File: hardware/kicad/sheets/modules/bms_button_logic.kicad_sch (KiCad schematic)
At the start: 13 parts, among them Q21 L2N7002SLLT1G, SW2 TL3305AF160QG, U61 NCP718ASN330T1G, U62 PMEG10030ELPX

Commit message: fixed bugs with bms sheets
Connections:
- net PB_3V3 renamed 3v3
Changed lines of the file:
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@@
+	(wire
+		(pts
+			(xy 101.6 80.01) (xy 113.03 80.01)
+		)
+		(stroke
+			(width 0)
+			(type default)
+		)
+	)
 	(wire
 		(pts
@@
 	(wire
 		(pts
+			(xy 113.03 78.74) (xy 113.03 80.01)
+		)
+		(stroke
+			(width 0)
+			(type default)
+		)
+	)
+	(wire
+		(pts
 			(xy 91.44 116.84) (xy 91.44 110.49)
 		)
@@
 	(wire
 		(pts
-			(xy 113.03 80.01) (xy 101.6 80.01)
-		)
-		(stroke
-			(width 0)
-			(type default)
-		)
-	)
-	(wire
-		(pts
 			(xy 91.44 110.49) (xy 113.03 110.49)
 		)
@@
 			(width 0)
 			(type default)
-		)
-	)
-	(label "PB_3V3"
-		(at 116.84 80.01 0)
-		(effects
-			(font
-				(size 1.27 1.27)
-			)
-			(justify left bottom)
 		)
 	)
@@
 		)
 	)
+	(hierarchical_label "3v3"
+		(shape output)
+		(at 113.03 78.74 90)
+		(effects
+			(font
+				(size 1.27 1.27)
+			)
+			(justify left)
+		)
+	)

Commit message: various improvements
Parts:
- renumbered C112 to C120, C115 to C121, C118 to C122, D35 to D43, Q21 to Q25, R162 to R182, R174 to R183, R177 to R184, R178 to R185, U61 to U62, U62 to U63
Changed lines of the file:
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@@
 		(on_board yes)
 		(dnp no)
-		(property "Reference" "R174"
+		(property "Reference" "R183"
 			(at 161.29 124.46 90)
 			(effects
@@
 			(project "svea_powerboard_rev3"
 				(path "/3f85abf4-0b95-4c4a-b7e9-06f59ca1ea3d/5c2e021f-c2d4-49e2-8c36-9a64f1f12001/261b4c59-ebc7-47a2-bb10-0e71ece0f9bf"
-					(reference "R174")
+					(reference "R183")
 					(unit 1)
 				)
@@
 		(on_board yes)
 		(dnp no)
-		(property "Reference" "D35"
+		(property "Reference" "D43"
 			(at 175.26 124.46 90)
 			(effects
@@
 			(project "svea_powerboard_rev3"
 				(path "/3f85abf4-0b95-4c4a-b7e9-06f59ca1ea3d/5c2e021f-c2d4-49e2-8c36-9a64f1f12001/261b4c59-ebc7-47a2-bb10-0e71ece0f9bf"
-					(reference "D35")
+					(reference "D43")
 					(unit 1)
 				)
@@
 		(on_board yes)
 		(dnp no)
-		(property "Reference" "R178"
+		(property "Reference" "R185"
 			(at 209.55 124.46 90)
 			(effects
@@
 			(project "svea_powerboard_rev3"
 				(path "/3f85abf4-0b95-4c4a-b7e9-06f59ca1ea3d/5c2e021f-c2d4-49e2-8c36-9a64f1f12001/261b4c59-ebc7-47a2-bb10-0e71ece0f9bf"
-					(reference "R178")
+					(reference "R185")
 					(unit 1)
 				)
@@
 		(on_board yes)
 		(dnp no)
-		(property "Reference" "C112"
+		(property "Reference" "C120"
 			(at 64.77 96.52 90)
 			(effects
@@
 			(project "svea_powerboard_rev3"
 				(path "/3f85abf4-0b95-4c4a-b7e9-06f59ca1ea3d/5c2e021f-c2d4-49e2-8c36-9a64f1f12001/261b4c59-ebc7-47a2-bb10-0e71ece0f9bf"
-					(reference "C112")
+					(reference "C120")
 					(unit 1)
 				)
@@
 		(on_board yes)
 		(dnp no)
-		(property "Reference" "U61"
+		(property "Reference" "U62"
 			(at 81.28 76.2 0)
 			(effects
@@
 			(project "svea_powerboard_rev3"
 				(path "/3f85abf4-0b95-4c4a-b7e9-06f59ca1ea3d/5c2e021f-c2d4-49e2-8c36-9a64f1f12001/261b4c59-ebc7-47a2-bb10-0e71ece0f9bf"
-					(reference "U61")
+					(reference "U62")
 					(unit 1)
 				)
@@
 		(on_board yes)
 		(dnp no)
-		(property "Reference" "R162"
+		(property "Reference" "R182"
 			(at 78.74 97.79 90)
 			(effects
@@
 			(project "svea_powerboard_rev3"
 				(path "/3f85abf4-0b95-4c4a-b7e9-06f59ca1ea3d/5c2e021f-c2d4-49e2-8c36-9a64f1f12001/261b4c59-ebc7-47a2-bb10-0e71ece0f9bf"
-					(reference "R162")
+					(reference "R182")
 					(unit 1)
 				)
@@
 		(on_board yes)
 		(dnp no)
-		(property "Reference" "C118"
+		(property "Reference" "C122"
 			(at 190.5 124.46 90)
 			(effects
@@
 			(project "svea_powerboard_rev3"
 				(path "/3f85abf4-0b95-4c4a-b7e9-06f59ca1ea3d/5c2e021f-c2d4-49e2-8c36-9a64f1f12001/261b4c59-ebc7-47a2-bb10-0e71ece0f9bf"
-					(reference "C118")
+					(reference "C122")
 					(unit 1)
 				)
@@
 		(on_board yes)
 		(dnp no)
-		(property "Reference" "U62"
+		(property "Reference" "U63"
 			(at 144.78 74.93 0)
 			(effects
@@
 			(project "svea_powerboard_rev3"
 				(path "/3f85abf4-0b95-4c4a-b7e9-06f59ca1ea3d/5c2e021f-c2d4-49e2-8c36-9a64f1f12001/261b4c59-ebc7-47a2-bb10-0e71ece0f9bf"
-					(reference "U62")
+					(reference "U63")
 					(unit 1)
 				)
@@
 		(on_board yes)
 		(dnp no)
-		(property "Reference" "R177"
+		(property "Reference" "R184"
 			(at 209.55 68.58 90)
 			(effects
@@
 			(project "svea_powerboard_rev3"
 				(path "/3f85abf4-0b95-4c4a-b7e9-06f59ca1ea3d/5c2e021f-c2d4-49e2-8c36-9a64f1f12001/261b4c59-ebc7-47a2-bb10-0e71ece0f9bf"
-					(reference "R177")
+					(reference "R184")
 					(unit 1)
 				)
@@
 		(on_board yes)
 		(dnp no)
-		(property "Reference" "C115"
+		(property "Reference" "C121"
 			(at 116.84 93.98 90)
 			(effects
@@
 			(project "svea_powerboard_rev3"
 				(path "/3f85abf4-0b95-4c4a-b7e9-06f59ca1ea3d/5c2e021f-c2d4-49e2-8c36-9a64f1f12001/261b4c59-ebc7-47a2-bb10-0e71ece0f9bf"
-					(reference "C115")
+					(reference "C121")
 					(unit 1)
 				)
@@
 		(on_board yes)
 		(dnp no)
-		(property "Reference" "Q21"
+		(property "Reference" "Q25"
 			(at 179.07 90.17 0)
 			(effects
@@
 			(project "svea_powerboard_rev3"
 				(path "/3f85abf4-0b95-4c4a-b7e9-06f59ca1ea3d/5c2e021f-c2d4-49e2-8c36-9a64f1f12001/261b4c59-ebc7-47a2-bb10-0e71ece0f9bf"
-					(reference "Q21")
+					(reference "Q25")
 					(unit 1)
 				)

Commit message: various improvements
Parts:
- renumbered C120 to C108, C121 to C113, C122 to C116, D43 to D32, Q25 to Q20, R182 to R162, R183 to R164, R184 to R166, R185 to R167, U62 to U63, U63 to U65
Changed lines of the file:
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@@
 		(on_board yes)
 		(dnp no)
-		(property "Reference" "R183"
+		(property "Reference" "R164"
 			(at 161.29 124.46 90)
 			(effects
@@
 			(project "svea_powerboard_rev3"
 				(path "/3f85abf4-0b95-4c4a-b7e9-06f59ca1ea3d/5c2e021f-c2d4-49e2-8c36-9a64f1f12001/261b4c59-ebc7-47a2-bb10-0e71ece0f9bf"
-					(reference "R183")
+					(reference "R164")
 					(unit 1)
 				)
@@
 		(on_board yes)
 		(dnp no)
-		(property "Reference" "D43"
+		(property "Reference" "D32"
 			(at 175.26 124.46 90)
 			(effects
@@
 			(project "svea_powerboard_rev3"
 				(path "/3f85abf4-0b95-4c4a-b7e9-06f59ca1ea3d/5c2e021f-c2d4-49e2-8c36-9a64f1f12001/261b4c59-ebc7-47a2-bb10-0e71ece0f9bf"
-					(reference "D43")
+					(reference "D32")
 					(unit 1)
 				)
@@
 		(on_board yes)
 		(dnp no)
-		(property "Reference" "R185"
+		(property "Reference" "R167"
 			(at 209.55 124.46 90)
 			(effects
@@
 			(project "svea_powerboard_rev3"
 				(path "/3f85abf4-0b95-4c4a-b7e9-06f59ca1ea3d/5c2e021f-c2d4-49e2-8c36-9a64f1f12001/261b4c59-ebc7-47a2-bb10-0e71ece0f9bf"
-					(reference "R185")
+					(reference "R167")
 					(unit 1)
 				)
@@
 		(on_board yes)
 		(dnp no)
-		(property "Reference" "C120"
+		(property "Reference" "C108"
 			(at 64.77 96.52 90)
 			(effects
@@
 			(project "svea_powerboard_rev3"
 				(path "/3f85abf4-0b95-4c4a-b7e9-06f59ca1ea3d/5c2e021f-c2d4-49e2-8c36-9a64f1f12001/261b4c59-ebc7-47a2-bb10-0e71ece0f9bf"
-					(reference "C120")
+					(reference "C108")
 					(unit 1)
 				)
@@
 		(on_board yes)
 		(dnp no)
-		(property "Reference" "U62"
+		(property "Reference" "U63"
 			(at 81.28 76.2 0)
 			(effects
@@
 			(project "svea_powerboard_rev3"
 				(path "/3f85abf4-0b95-4c4a-b7e9-06f59ca1ea3d/5c2e021f-c2d4-49e2-8c36-9a64f1f12001/261b4c59-ebc7-47a2-bb10-0e71ece0f9bf"
-					(reference "U62")
+					(reference "U63")
 					(unit 1)
 				)
@@
 		(on_board yes)
 		(dnp no)
-		(property "Reference" "R182"
+		(property "Reference" "R162"
 			(at 78.74 97.79 90)
 			(effects
@@
 			(project "svea_powerboard_rev3"
 				(path "/3f85abf4-0b95-4c4a-b7e9-06f59ca1ea3d/5c2e021f-c2d4-49e2-8c36-9a64f1f12001/261b4c59-ebc7-47a2-bb10-0e71ece0f9bf"
-					(reference "R182")
+					(reference "R162")
 					(unit 1)
 				)
@@
 		(on_board yes)
 		(dnp no)
-		(property "Reference" "C122"
+		(property "Reference" "C116"
 			(at 190.5 124.46 90)
 			(effects
@@
 			(project "svea_powerboard_rev3"
 				(path "/3f85abf4-0b95-4c4a-b7e9-06f59ca1ea3d/5c2e021f-c2d4-49e2-8c36-9a64f1f12001/261b4c59-ebc7-47a2-bb10-0e71ece0f9bf"
-					(reference "C122")
+					(reference "C116")
 					(unit 1)
 				)
@@
 		(on_board yes)
 		(dnp no)
-		(property "Reference" "U63"
+		(property "Reference" "U65"
 			(at 144.78 74.93 0)
 			(effects
@@
 			(project "svea_powerboard_rev3"
 				(path "/3f85abf4-0b95-4c4a-b7e9-06f59ca1ea3d/5c2e021f-c2d4-49e2-8c36-9a64f1f12001/261b4c59-ebc7-47a2-bb10-0e71ece0f9bf"
-					(reference "U63")
+					(reference "U65")
 					(unit 1)
 				)
@@
 		(on_board yes)
 		(dnp no)
-		(property "Reference" "R184"
+		(property "Reference" "R166"
 			(at 209.55 68.58 90)
 			(effects
@@
 			(project "svea_powerboard_rev3"
 				(path "/3f85abf4-0b95-4c4a-b7e9-06f59ca1ea3d/5c2e021f-c2d4-49e2-8c36-9a64f1f12001/261b4c59-ebc7-47a2-bb10-0e71ece0f9bf"
-					(reference "R184")
+					(reference "R166")
 					(unit 1)
 				)
@@
 		(on_board yes)
 		(dnp no)
-		(property "Reference" "C121"
+		(property "Reference" "C113"
 			(at 116.84 93.98 90)
 			(effects
@@
 			(project "svea_powerboard_rev3"
 				(path "/3f85abf4-0b95-4c4a-b7e9-06f59ca1ea3d/5c2e021f-c2d4-49e2-8c36-9a64f1f12001/261b4c59-ebc7-47a2-bb10-0e71ece0f9bf"
-					(reference "C121")
+					(reference "C113")
 					(unit 1)
 				)
@@
 		(on_board yes)
 		(dnp no)
-		(property "Reference" "Q25"
+		(property "Reference" "Q20"
 			(at 179.07 90.17 0)
 			(effects
@@
 			(project "svea_powerboard_rev3"
 				(path "/3f85abf4-0b95-4c4a-b7e9-06f59ca1ea3d/5c2e021f-c2d4-49e2-8c36-9a64f1f12001/261b4c59-ebc7-47a2-bb10-0e71ece0f9bf"
-					(reference "Q25")
+					(reference "Q20")
 					(unit 1)
 				)

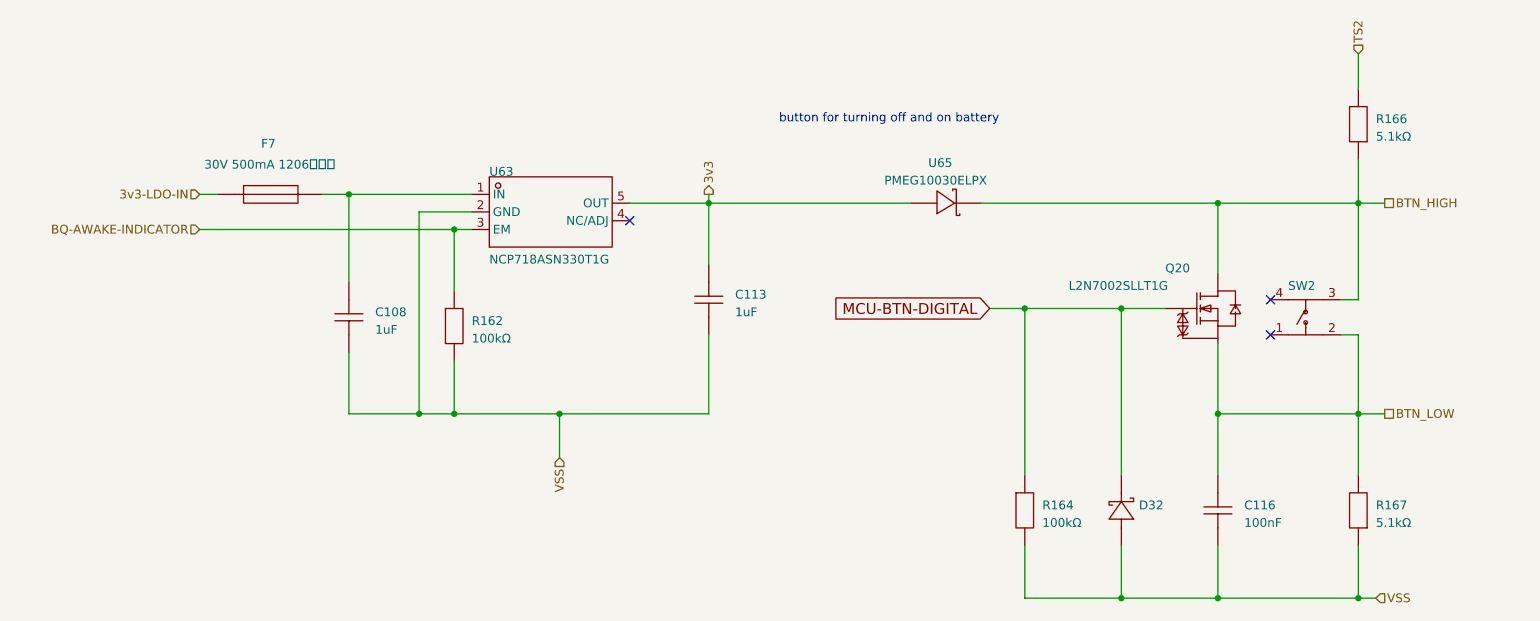
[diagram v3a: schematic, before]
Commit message: current sensing on the servos and cleaning up empty sheets
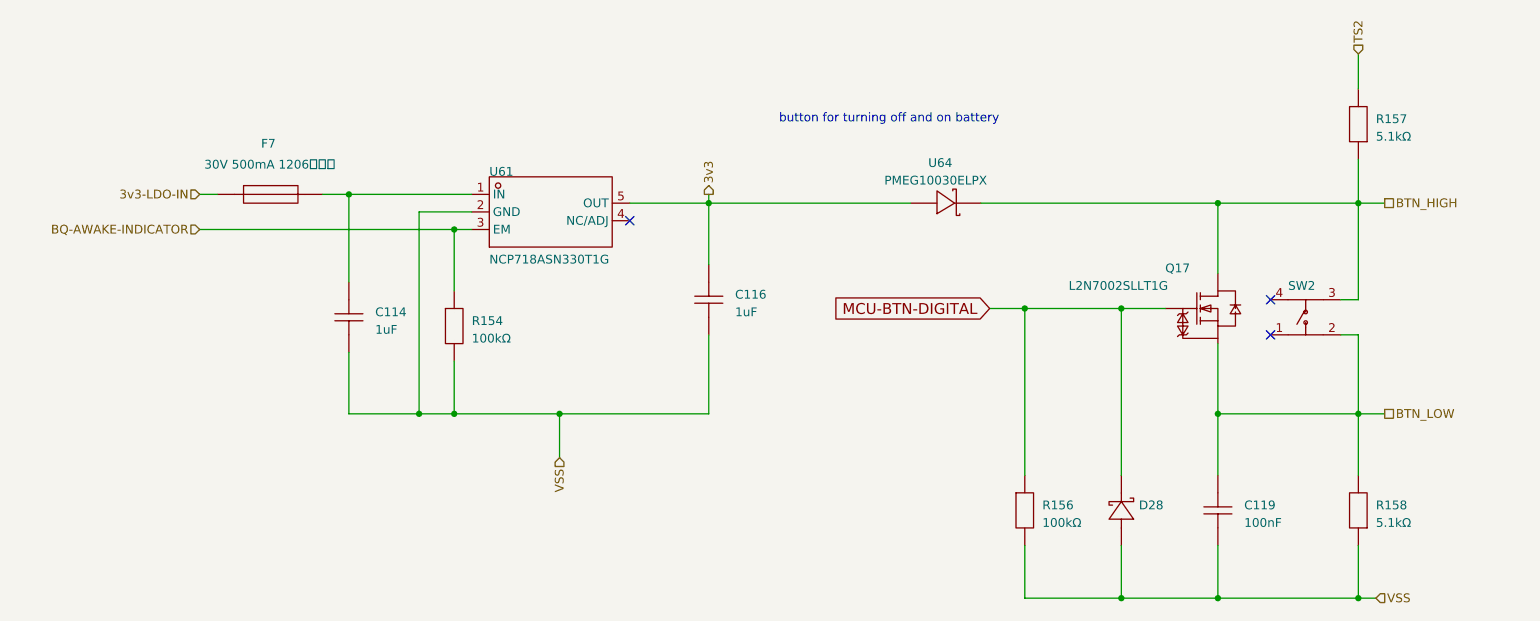
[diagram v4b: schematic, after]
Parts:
- renumbered C108 to C114, C113 to C116, C116 to C119, D32 to D28, Q20 to Q17, R162 to R154, R164 to R156, R166 to R157, R167 to R158, U63 to U61, U65 to U64
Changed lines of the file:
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@@
 		(on_board yes)
 		(dnp no)
-		(property "Reference" "R164"
+		(property "Reference" "R156"
 			(at 161.29 124.46 90)
 			(effects
@@
 			(project "svea_powerboard_rev3"
 				(path "/3f85abf4-0b95-4c4a-b7e9-06f59ca1ea3d/5c2e021f-c2d4-49e2-8c36-9a64f1f12001/261b4c59-ebc7-47a2-bb10-0e71ece0f9bf"
-					(reference "R164")
+					(reference "R156")
 					(unit 1)
 				)
@@
 		(on_board yes)
 		(dnp no)
-		(property "Reference" "D32"
+		(property "Reference" "D28"
 			(at 175.26 124.46 90)
 			(effects
@@
 			(project "svea_powerboard_rev3"
 				(path "/3f85abf4-0b95-4c4a-b7e9-06f59ca1ea3d/5c2e021f-c2d4-49e2-8c36-9a64f1f12001/261b4c59-ebc7-47a2-bb10-0e71ece0f9bf"
-					(reference "D32")
+					(reference "D28")
 					(unit 1)
 				)
@@
 		(on_board yes)
 		(dnp no)
-		(property "Reference" "R167"
+		(property "Reference" "R158"
 			(at 209.55 124.46 90)
 			(effects
@@
 			(project "svea_powerboard_rev3"
 				(path "/3f85abf4-0b95-4c4a-b7e9-06f59ca1ea3d/5c2e021f-c2d4-49e2-8c36-9a64f1f12001/261b4c59-ebc7-47a2-bb10-0e71ece0f9bf"
-					(reference "R167")
+					(reference "R158")
 					(unit 1)
 				)
@@
 		(on_board yes)
 		(dnp no)
-		(property "Reference" "C108"
+		(property "Reference" "C114"
 			(at 64.77 96.52 90)
 			(effects
@@
 			(project "svea_powerboard_rev3"
 				(path "/3f85abf4-0b95-4c4a-b7e9-06f59ca1ea3d/5c2e021f-c2d4-49e2-8c36-9a64f1f12001/261b4c59-ebc7-47a2-bb10-0e71ece0f9bf"
-					(reference "C108")
+					(reference "C114")
 					(unit 1)
 				)
@@
 		(on_board yes)
 		(dnp no)
-		(property "Reference" "U63"
+		(property "Reference" "U61"
 			(at 81.28 76.2 0)
 			(effects
@@
 			(project "svea_powerboard_rev3"
 				(path "/3f85abf4-0b95-4c4a-b7e9-06f59ca1ea3d/5c2e021f-c2d4-49e2-8c36-9a64f1f12001/261b4c59-ebc7-47a2-bb10-0e71ece0f9bf"
-					(reference "U63")
+					(reference "U61")
 					(unit 1)
 				)
@@
 		(on_board yes)
 		(dnp no)
-		(property "Reference" "R162"
+		(property "Reference" "R154"
 			(at 78.74 97.79 90)
 			(effects
@@
 			(project "svea_powerboard_rev3"
 				(path "/3f85abf4-0b95-4c4a-b7e9-06f59ca1ea3d/5c2e021f-c2d4-49e2-8c36-9a64f1f12001/261b4c59-ebc7-47a2-bb10-0e71ece0f9bf"
-					(reference "R162")
+					(reference "R154")
 					(unit 1)
 				)
@@
 		(on_board yes)
 		(dnp no)
-		(property "Reference" "C116"
+		(property "Reference" "C119"
 			(at 190.5 124.46 90)
 			(effects
@@
 			(project "svea_powerboard_rev3"
 				(path "/3f85abf4-0b95-4c4a-b7e9-06f59ca1ea3d/5c2e021f-c2d4-49e2-8c36-9a64f1f12001/261b4c59-ebc7-47a2-bb10-0e71ece0f9bf"
-					(reference "C116")
+					(reference "C119")
 					(unit 1)
 				)
@@
 		(on_board yes)
 		(dnp no)
-		(property "Reference" "U65"
+		(property "Reference" "U64"
 			(at 144.78 74.93 0)
 			(effects
@@
 			(project "svea_powerboard_rev3"
 				(path "/3f85abf4-0b95-4c4a-b7e9-06f59ca1ea3d/5c2e021f-c2d4-49e2-8c36-9a64f1f12001/261b4c59-ebc7-47a2-bb10-0e71ece0f9bf"
-					(reference "U65")
+					(reference "U64")
 					(unit 1)
 				)
@@
 		(on_board yes)
 		(dnp no)
-		(property "Reference" "R166"
+		(property "Reference" "R157"
 			(at 209.55 68.58 90)
 			(effects
@@
 			(project "svea_powerboard_rev3"
 				(path "/3f85abf4-0b95-4c4a-b7e9-06f59ca1ea3d/5c2e021f-c2d4-49e2-8c36-9a64f1f12001/261b4c59-ebc7-47a2-bb10-0e71ece0f9bf"
-					(reference "R166")
+					(reference "R157")
 					(unit 1)
 				)
@@
 		(on_board yes)
 		(dnp no)
-		(property "Reference" "C113"
+		(property "Reference" "C116"
 			(at 116.84 93.98 90)
 			(effects
@@
 			(project "svea_powerboard_rev3"
 				(path "/3f85abf4-0b95-4c4a-b7e9-06f59ca1ea3d/5c2e021f-c2d4-49e2-8c36-9a64f1f12001/261b4c59-ebc7-47a2-bb10-0e71ece0f9bf"
-					(reference "C113")
+					(reference "C116")
 					(unit 1)
 				)
@@
 		(on_board yes)
 		(dnp no)
-		(property "Reference" "Q20"
+		(property "Reference" "Q17"
 			(at 179.07 90.17 0)
 			(effects
@@
 			(project "svea_powerboard_rev3"
 				(path "/3f85abf4-0b95-4c4a-b7e9-06f59ca1ea3d/5c2e021f-c2d4-49e2-8c36-9a64f1f12001/261b4c59-ebc7-47a2-bb10-0e71ece0f9bf"
-					(reference "Q20")
+					(reference "Q17")
 					(unit 1)
 				)

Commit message: new references
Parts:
- renumbered C114 to C129, C116 to C131, C119 to C133, D28 to D38, F7 to F5, Q17 to Q18, R154 to R177, R156 to R178, R157 to R179, R158 to R180, SW2 to SW1, U64 to U63
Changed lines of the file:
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@@
 		(on_board yes)
 		(dnp no)
-		(property "Reference" "R156"
+		(property "Reference" "R178"
 			(at 161.29 124.46 90)
 			(effects
@@
 			(project "svea_powerboard_rev3"
 				(path "/3f85abf4-0b95-4c4a-b7e9-06f59ca1ea3d/5c2e021f-c2d4-49e2-8c36-9a64f1f12001/261b4c59-ebc7-47a2-bb10-0e71ece0f9bf"
-					(reference "R156")
+					(reference "R178")
 					(unit 1)
 				)
@@
 		(on_board yes)
 		(dnp no)
-		(property "Reference" "SW2"
+		(property "Reference" "SW1"
 			(at 196.85 92.71 0)
 			(effects
@@
 			(project "svea_powerboard_rev3"
 				(path "/3f85abf4-0b95-4c4a-b7e9-06f59ca1ea3d/5c2e021f-c2d4-49e2-8c36-9a64f1f12001/261b4c59-ebc7-47a2-bb10-0e71ece0f9bf"
-					(reference "SW2")
+					(reference "SW1")
 					(unit 1)
 				)
@@
 		(on_board yes)
 		(dnp no)
-		(property "Reference" "D28"
+		(property "Reference" "D38"
 			(at 175.26 124.46 90)
 			(effects
@@
 			(project "svea_powerboard_rev3"
 				(path "/3f85abf4-0b95-4c4a-b7e9-06f59ca1ea3d/5c2e021f-c2d4-49e2-8c36-9a64f1f12001/261b4c59-ebc7-47a2-bb10-0e71ece0f9bf"
-					(reference "D28")
+					(reference "D38")
 					(unit 1)
 				)
@@
 		(on_board yes)
 		(dnp no)
-		(property "Reference" "R158"
+		(property "Reference" "R180"
 			(at 209.55 124.46 90)
 			(effects
@@
 			(project "svea_powerboard_rev3"
 				(path "/3f85abf4-0b95-4c4a-b7e9-06f59ca1ea3d/5c2e021f-c2d4-49e2-8c36-9a64f1f12001/261b4c59-ebc7-47a2-bb10-0e71ece0f9bf"
-					(reference "R158")
+					(reference "R180")
 					(unit 1)
 				)
@@
 		(on_board yes)
 		(dnp no)
-		(property "Reference" "C114"
+		(property "Reference" "C129"
 			(at 64.77 96.52 90)
 			(effects
@@
 			(project "svea_powerboard_rev3"
 				(path "/3f85abf4-0b95-4c4a-b7e9-06f59ca1ea3d/5c2e021f-c2d4-49e2-8c36-9a64f1f12001/261b4c59-ebc7-47a2-bb10-0e71ece0f9bf"
-					(reference "C114")
+					(reference "C129")
 					(unit 1)
 				)
@@
 		(on_board yes)
 		(dnp no)
-		(property "Reference" "R154"
+		(property "Reference" "R177"
 			(at 78.74 97.79 90)
 			(effects
@@
 			(project "svea_powerboard_rev3"
 				(path "/3f85abf4-0b95-4c4a-b7e9-06f59ca1ea3d/5c2e021f-c2d4-49e2-8c36-9a64f1f12001/261b4c59-ebc7-47a2-bb10-0e71ece0f9bf"
-					(reference "R154")
+					(reference "R177")
 					(unit 1)
 				)
@@
 		(on_board yes)
 		(dnp no)
-		(property "Reference" "C119"
+		(property "Reference" "C133"
 			(at 190.5 124.46 90)
 			(effects
@@
 			(project "svea_powerboard_rev3"
 				(path "/3f85abf4-0b95-4c4a-b7e9-06f59ca1ea3d/5c2e021f-c2d4-49e2-8c36-9a64f1f12001/261b4c59-ebc7-47a2-bb10-0e71ece0f9bf"
-					(reference "C119")
+					(reference "C133")
 					(unit 1)
 				)
@@
 		(on_board yes)
 		(dnp no)
-		(property "Reference" "F7"
+		(property "Reference" "F5"
 			(at 48.26 72.136 0)
 			(effects
@@
 			(project "svea_powerboard_rev3"
 				(path "/3f85abf4-0b95-4c4a-b7e9-06f59ca1ea3d/5c2e021f-c2d4-49e2-8c36-9a64f1f12001/261b4c59-ebc7-47a2-bb10-0e71ece0f9bf"
-					(reference "F7")
+					(reference "F5")
 					(unit 1)
 				)
@@
 		(on_board yes)
 		(dnp no)
-		(property "Reference" "U64"
+		(property "Reference" "U63"
 			(at 144.78 74.93 0)
 			(effects
@@
 			(project "svea_powerboard_rev3"
 				(path "/3f85abf4-0b95-4c4a-b7e9-06f59ca1ea3d/5c2e021f-c2d4-49e2-8c36-9a64f1f12001/261b4c59-ebc7-47a2-bb10-0e71ece0f9bf"
-					(reference "U64")
+					(reference "U63")
 					(unit 1)
 				)
@@
 		(on_board yes)
 		(dnp no)
-		(property "Reference" "R157"
+		(property "Reference" "R179"
 			(at 209.55 68.58 90)
 			(effects
@@
 			(project "svea_powerboard_rev3"
 				(path "/3f85abf4-0b95-4c4a-b7e9-06f59ca1ea3d/5c2e021f-c2d4-49e2-8c36-9a64f1f12001/261b4c59-ebc7-47a2-bb10-0e71ece0f9bf"
-					(reference "R157")
+					(reference "R179")
 					(unit 1)
 				)
@@
 		(on_board yes)
 		(dnp no)
-		(property "Reference" "C116"
+		(property "Reference" "C131"
 			(at 116.84 93.98 90)
 			(effects
@@
 			(project "svea_powerboard_rev3"
 				(path "/3f85abf4-0b95-4c4a-b7e9-06f59ca1ea3d/5c2e021f-c2d4-49e2-8c36-9a64f1f12001/261b4c59-ebc7-47a2-bb10-0e71ece0f9bf"
-					(reference "C116")
+					(reference "C131")
 					(unit 1)
 				)
@@
 		(on_board yes)
 		(dnp no)
-		(property "Reference" "Q17"
+		(property "Reference" "Q18"
 			(at 179.07 90.17 0)
 			(effects
@@
 			(project "svea_powerboard_rev3"
 				(path "/3f85abf4-0b95-4c4a-b7e9-06f59ca1ea3d/5c2e021f-c2d4-49e2-8c36-9a64f1f12001/261b4c59-ebc7-47a2-bb10-0e71ece0f9bf"
-					(reference "Q17")
+					(reference "Q18")
 					(unit 1)
 				)
